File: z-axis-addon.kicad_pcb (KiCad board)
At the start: 2 copper layers, 68.6 x 48.4 mm, 11 parts, among them J1 Conn_01x06_Socket, J2 Conn_01x08_Socket, J3 Conn_01x03_Socket, J4 Conn_01x04_Socket, U1 TMC2130

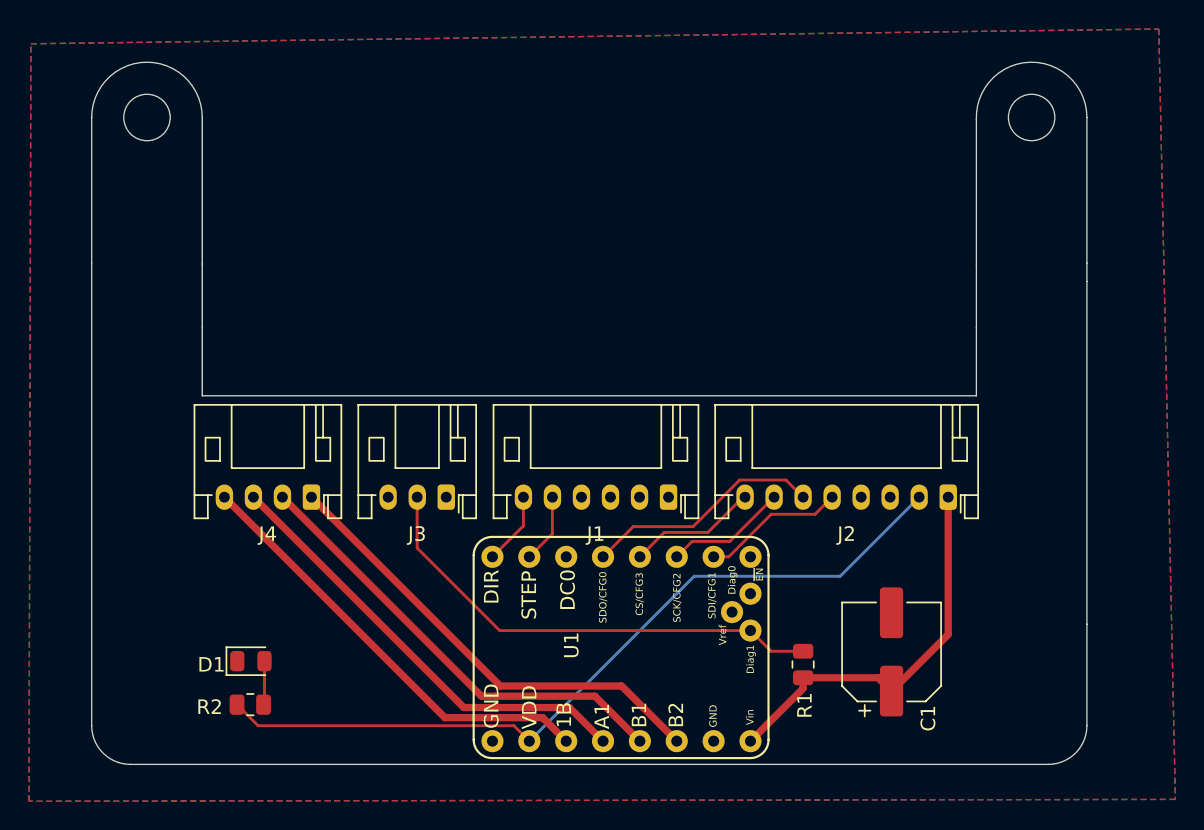
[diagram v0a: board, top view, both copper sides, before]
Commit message: Update text on PCB
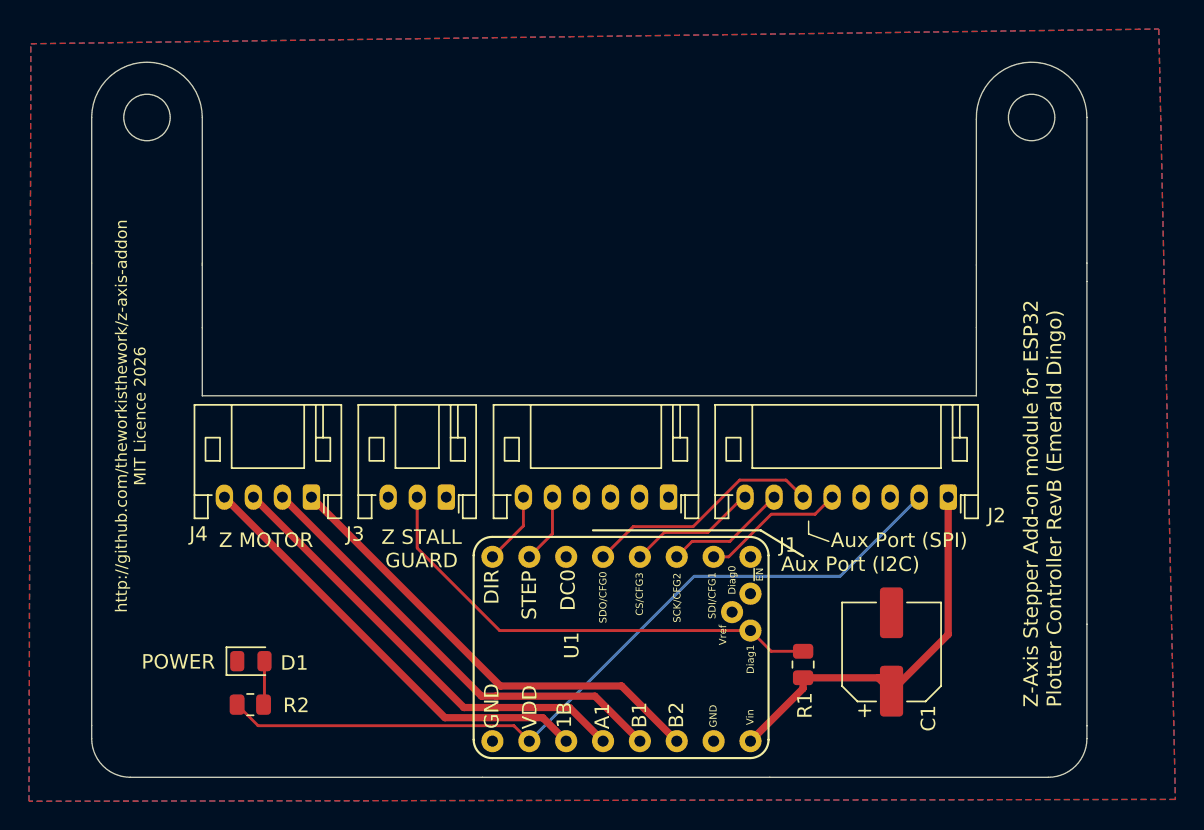
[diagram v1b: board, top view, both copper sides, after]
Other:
- board size 68.6 x 48.4 mm -> 68.6 x 49.3 mm
- board text added: "Aux Port (I2C)"
- board text added: "Aux Port (SPI)"
- board text added: "POWER"
- board text added: "Z MOTOR"
- board text added: "Z STALL GUARD"
- board text added: "Z-Axis Stepper Add-on module for ESP32 Plotter Controller RevB (Emerald Dingo)"
- board text added: "http://github.com/theworkisthework/z-axis-addon MIT Licence 2026"
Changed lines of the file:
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@@
 			(fill no)
 			(layer "Cmts.User")
+			(net 2)
 		)
 		(fp_circle
@@
 			(fill no)
 			(layer "F.CrtYd")
+			(net 2)
 		)
 		(fp_text user "H3"
@@
 		(tags "resistor")
 		(property "Reference" "R2"
-			(at -2.8025 0.18 0)
+			(at 3.1665 0.053 0)
 			(layer "F.SilkS")
 			(effects
@@
 		(tags "LED")
 		(property "Reference" "D1"
-			(at -2.7155 0.254 0)
+			(at 2.9995 0.127 0)
 			(layer "F.SilkS")
 			(effects
@@
 		(tags "connector JST PH horizontal")
 		(property "Reference" "J1"
-			(at 5 -2.55 0)
+			(at -8.256 -3.302 0)
 			(layer "F.SilkS")
 			(effects
@@
 		(tags "connector JST PH horizontal")
 		(property "Reference" "J3"
-			(at 2 -2.55 0)
+			(at 6.27 -2.55 0)
 			(layer "F.SilkS")
 			(effects
@@
 		(tags "connector JST PH horizontal")
 		(property "Reference" "J2"
-			(at 7 -2.55 180)
+			(at -3.335 -1.27 180)
 			(layer "F.SilkS")
 			(effects
@@
 		(tags "connector JST PH horizontal")
 		(property "Reference" "J4"
-			(at 3 -2.55 0)
+			(at 7.778 -2.54 0)
 			(layer "F.SilkS")
 			(effects
@@
 			(fill no)
 			(layer "Cmts.User")
+			(net 2)
 		)
 		(fp_circle
@@
 			(fill no)
 			(layer "F.CrtYd")
+			(net 2)
 		)
 		(fp_text user "${REFERENCE}"
@@
 	)
 	(gr_line
+		(start 203.454 122.682)
+		(end 202.057 122.174)
+		(stroke
+			(width 0.1)
+			(type default)
+		)
+		(layer "F.SilkS")
+	)
+	(gr_line
+		(start 202.057 122.174)
+		(end 202.057 121.285)
+		(stroke
+			(width 0.1)
+			(type default)
+		)
+		(layer "F.SilkS")
+	)
+	(gr_line
+		(start 198.755 121.92)
+		(end 187.198 121.92)
+		(stroke
+			(width 0.15)
+			(type solid)
+		)
+		(layer "F.SilkS")
+	)
+	(gr_line
+		(start 201.676 123.698)
+		(end 198.755 121.92)
+		(stroke
+			(width 0.15)
+			(type solid)
+		)
+		(layer "F.SilkS")
+	)
+	(gr_line
 		(start 221.233999 93.472)
 		(end 221.234 103.505)
@@
 	)
 	(gr_arc
-		(start 221.234 135.382)
-		(mid 220.452854 137.267854)
-		(end 218.567 138.049)
+		(start 221.234 136.271)
+		(mid 220.452854 138.156854)
+		(end 218.567 138.938)
+		(stroke
+			(width 0.05)
+			(type default)
+		)
+		(layer "Edge.Cuts")
+	)
+	(gr_line
+		(start 221.234 136.271)
+		(end 221.234 135.382)
 		(stroke
 			(width 0.05)
@@
 		(layer "Edge.Cuts")
 	)
+	(gr_line
+		(start 152.654 136.271)
+		(end 152.654 135.382)
+		(stroke
+			(width 0.05)
+			(type default)
+		)
+		(layer "Edge.Cuts")
+	)
 	(gr_arc
 		(start 213.616115 93.59893)
@@
 	)
 	(gr_line
-		(start 218.567 138.049)
-		(end 199.39 138.049)
+		(start 218.567 138.938)
+		(end 199.39 138.938)
 		(stroke
 			(width 0.05)
@@
 	)
 	(gr_arc
-		(start 155.321 138.049)
-		(mid 153.435146 137.267854)
-		(end 152.654 135.382)
+		(start 155.321 138.938)
+		(mid 153.435146 138.156854)
+		(end 152.654 136.271)
 		(stroke
 			(width 0.05)
@@
 	)
 	(gr_line
-		(start 179.578 138.049)
-		(end 155.321 138.049)
+		(start 179.578 138.938)
+		(end 155.321 138.938)
 		(stroke
 			(width 0.05)
@@
 	)
 	(gr_line
-		(start 199.39 138.049)
-		(end 179.578 138.049)
+		(start 199.39 138.938)
+		(end 179.578 138.938)
 		(stroke
 			(width 0.05)
@@
 		(layer "Edge.Cuts")
 	)
+	(gr_text "Z-Axis Stepper Add-on module for ESP32 \nPlotter Controller RevB (Emerald Dingo)"
+		(at 219.583 134.112 90)
+		(layer "F.SilkS")
+		(effects
+			(font
+				(size 1 1)
+				(thickness 0.1)
+			)
+			(justify left bottom)
+		)
+	)
+	(gr_text "Aux Port (SPI)"
+		(at 203.581 123.19 0)
+		(layer "F.SilkS")
+		(effects
+			(font
+				(size 1 1)
+				(thickness 0.15)
+			)
+			(justify left bottom)
+		)
+	)
+	(gr_text "Z STALL\nGUARD"
+		(at 175.387 124.587 0)
+		(layer "F.SilkS")
+		(effects
+			(font
+				(size 1 1)
+				(thickness 0.15)
+			)
+			(justify bottom)
+		)
+	)
+	(gr_text "Z MOTOR"
+		(at 161.417 123.19 0)
+		(layer "F.SilkS")
+		(effects
+			(font
+				(size 1 1)
+				(thickness 0.15)
+			)
+			(justify left bottom)
+		)
+	)
+	(gr_text "http://github.com/theworkisthework/z-axis-addon\nMIT Licence 2026"
+		(at 156.464 114.046 90)
+		(layer "F.SilkS")
+		(effects
+			(font
+				(size 0.8 0.8)
+				(thickness 0.1)
+			)
+			(justify bottom)
+		)
+	)
+	(gr_text "POWER"
+		(at 156.083 131.572 0)
+		(layer "F.SilkS")
+		(effects
+			(font
+				(size 1 1)
+				(thickness 0.15)
+			)
+			(justify left bottom)
+		)
+	)
+	(gr_text "Aux Port (I2C)"
+		(at 200.152 124.841 0)
+		(layer "F.SilkS")
+		(effects
+			(font
+				(size 1 1)
+				(thickness 0.15)
+			)
+			(justify left bottom)
+		)
+	)
 	(segment
